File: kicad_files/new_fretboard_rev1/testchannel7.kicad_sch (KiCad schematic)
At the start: 22 parts, among them U2 LX3302AQPW-TR-EASY

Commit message: all circuit traces
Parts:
- removed C12, C13: 680pf, Capacitor_SMD:C_0603_1608Metric, symbol Device:C
- removed C14, C15: 10pf, Capacitor_SMD:C_0402_1005Metric, symbol Device:C
- removed C16: 1uf, Capacitor_SMD:C_0603_1608Metric, symbol Device:C
- removed C17, C20: 100nf, Capacitor_SMD:C_0402_1005Metric, symbol Device:C
- removed C18, C19: 6.8nf, Capacitor_SMD:C_0402_1005Metric, symbol Device:C
- removed C21: 1000pf, Capacitor_SMD:C_0402_1005Metric, symbol Device:C
- removed C22: 470nf, Capacitor_SMD:C_0402_1005Metric, symbol Device:C
- removed L5, L6, L7, L8: L, NetTie:NetTie-2_SMD_Pad0.5mm, symbol Device:L
- removed R10, R11, R8, R9: 10R, Resistor_SMD:R_0402_1005Metric, symbol Device:R
- removed R12: 221R, Resistor_SMD:R_0402_1005Metric, symbol Device:R
- removed R13: 4.7R, Resistor_SMD:R_0402_1005Metric, symbol Device:R
- removed U2: LX3302AQPW-TR-EASY, Snapeda:14-TSSOP_MCH-L, symbol Snapeda:LX3302AQPW-TR-EASY
- added C78, C84: 100nf, Capacitor_SMD:C_0402_1005Metric, symbol Device:C
- added C79: 1000pf, Capacitor_SMD:C_0402_1005Metric, symbol Device:C
- added C80: 470nf, Capacitor_SMD:C_0402_1005Metric, symbol Device:C
- added C81: 1uf, Capacitor_SMD:C_0603_1608Metric, symbol Device:C
- added C82, C83: 6.8nf, Capacitor_SMD:C_0402_1005Metric, symbol Device:C
- added C85, C86: 10pf, Capacitor_SMD:C_0402_1005Metric, symbol Device:C
- added C87, C88: 680pf, Capacitor_SMD:C_0603_1608Metric, symbol Device:C
- added L29, L30, L31, L32: L, NetTie:NetTie-2_SMD_Pad0.5mm, symbol Device:L
- added R43: 4.7R, Resistor_SMD:R_0402_1005Metric, symbol Device:R
- added R44: 221R, Resistor_SMD:R_0402_1005Metric, symbol Device:R
- added R45, R46, R47, R48: 10R, Resistor_SMD:R_0402_1005Metric, symbol Device:R
- added U8: LX3302AQPW-TR-EASY, Snapeda:14-TSSOP_MCH-L, symbol Snapeda:LX3302AQPW-TR-EASY
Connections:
- net CL1B_A: now also L32.1, R48.2
- net CL1_A: now also C85.1, R48.1, U8.8 (CL1)
- net CL2B_A: now also L31.1, R47.2
- net CL2_A: now also C86.1, R47.1, U8.10 (CL2)
- net GND: now also C78.1, C79.1, C80.1, C81.1, C82.1, C83.1, C85.2, C86.2, C87.2, C88.2, L31.2, L32.2, U8.2 (GND), U8.9 (GNDCL)
- net OSC11_A: now also C87.1, L29.2, U8.13 (OSC1)
- net OSC12_A: now also C88.1, L30.2, U8.12 (OSC2)
- net SUB_A: now also C84.1, U8.11 (SUB)
- net VIN_A: now also C79.2, C80.2, R43.1, R45.2, R46.1, U8.4 (VIN)
- new net: C81.2, C84.2, U8.5 (VDD)
- new net: C78.2, R43.2
- new net: C83.2, R44.1, R45.1, U8.6 (IO2)
- new net: C82.2, R44.2
- new net /OSC2B_A: L29.1, L30.1, R46.2
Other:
- removed sheet testchannel1
- removed sheet testchannel2
- removed sheet testchannel3
- removed sheet testchannel4
- removed sheet testchannel5
- removed sheet testchannel6
- removed sheet testchannel7

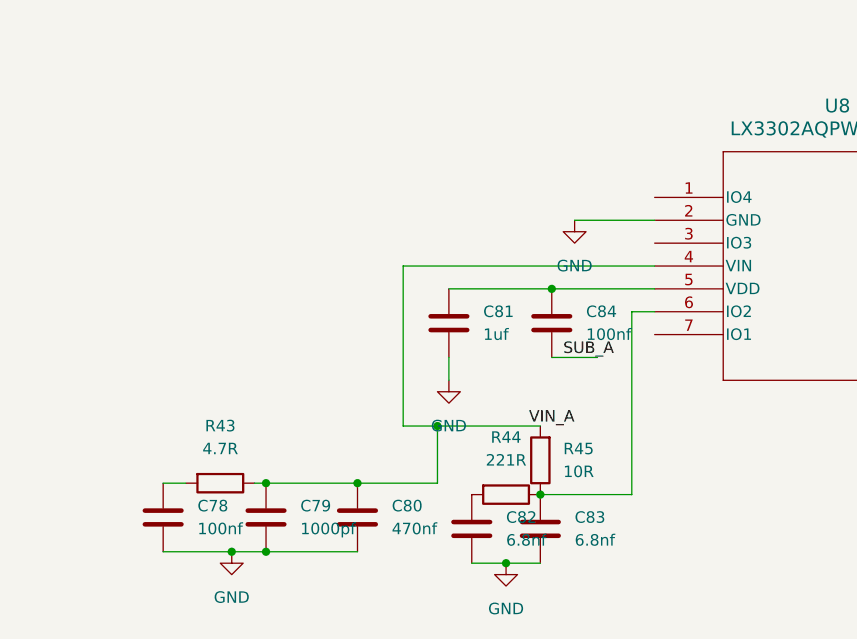
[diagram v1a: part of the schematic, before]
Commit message: stm32 micro added
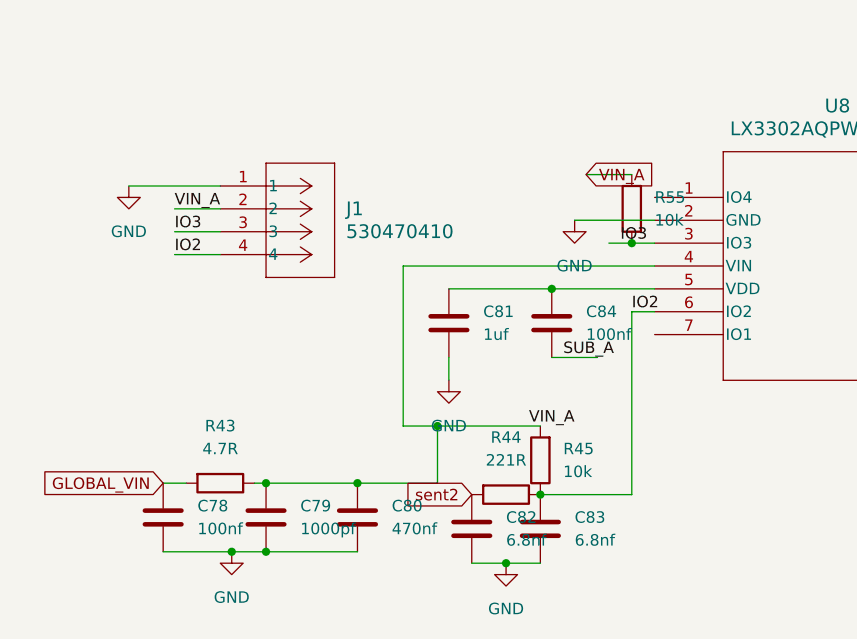
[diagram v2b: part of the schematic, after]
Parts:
- added J1: 530470410, Snapeda:CONN04_530470410_MOL, symbol Snapeda:530470410
- added R55: 10k, Resistor_SMD:R_0402_1005Metric, symbol Device:R
- R45: value 10R -> 10k
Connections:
- net GND: now also J1.1
- net VIN_A: now also J1.2, R55.2
- net GLOBAL_VIN: now reaches C78.2, R43.2
- net IO3: now reaches U8.3 (IO3)
- net IO3: now also J1.3, R55.1
- net IO2: now reaches C83.2, R44.1, R45.1, U8.6 (IO2)
- net IO2: now also J1.4
- net sent2: now reaches C82.2, R44.2

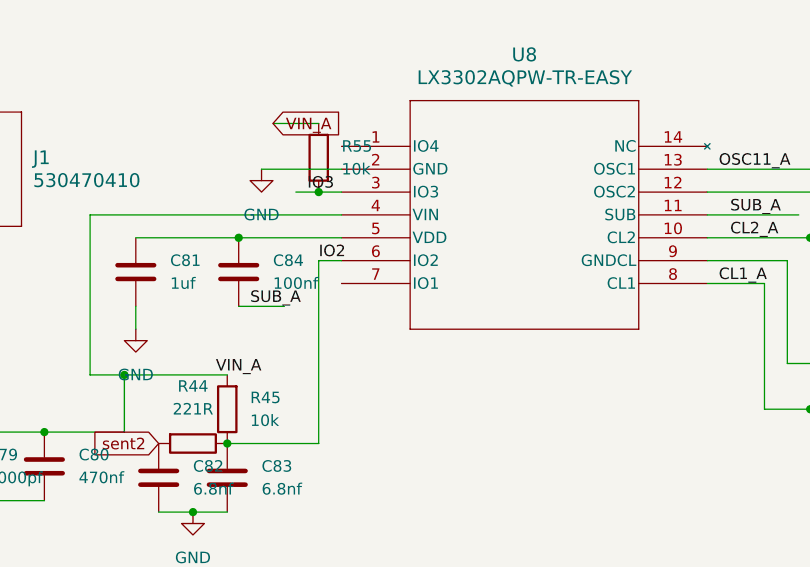
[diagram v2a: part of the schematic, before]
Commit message: mcu configured, still needs power connections and spi i2c connections
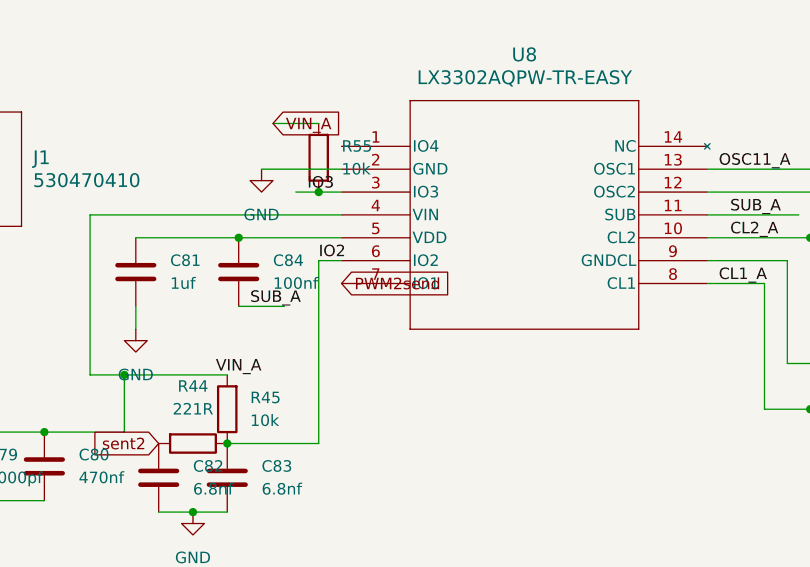
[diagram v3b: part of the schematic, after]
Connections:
- net PWM2send: now reaches U8.7 (IO1)
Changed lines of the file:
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@@
+		)
+	)
+	(global_label "PWM2send"
+		(shape input)
+		(at 104.14 106.68 0)
+		(fields_autoplaced yes)
+		(effects
+			(font
+				(size 1.27 1.27)
+			)
+			(justify left)
+		)
+		(property "Intersheetrefs" "${INTERSHEET_REFS}"
+			(at 116.9222 106.68 0)
+			(effects
+				(font
+					(size 1.27 1.27)
+				)
+				(justify left)
+				(hide yes)
+			)
 		)
 	)

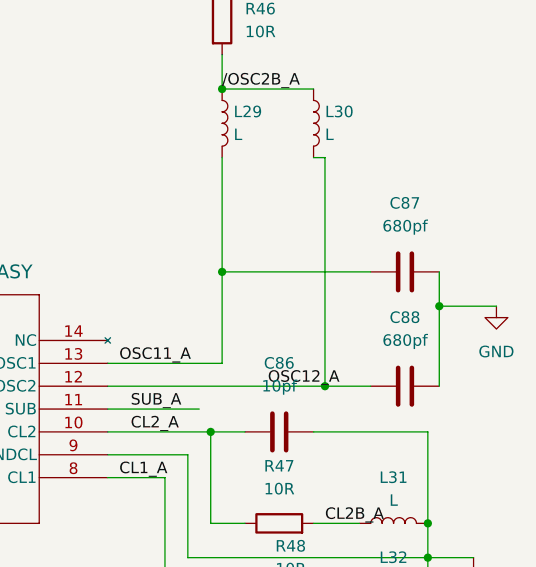
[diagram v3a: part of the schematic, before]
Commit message: finished routing - adding silkscreen
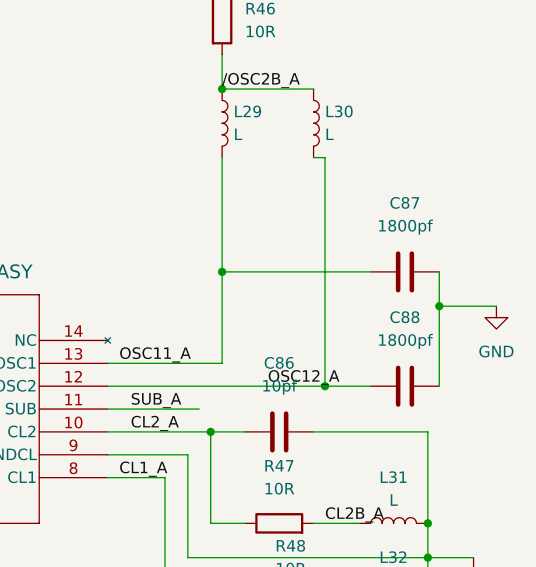
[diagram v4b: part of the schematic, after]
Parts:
- C87, C88: value 680pf -> 1800pf
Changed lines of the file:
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@@
 			)
 		)
-		(property "Value" "680pf"
+		(property "Value" "1800pf"
 			(at 177.8 78.74 90)
 			(effects
@@
 			)
 		)
-		(property "Value" "680pf"
+		(property "Value" "1800pf"
 			(at 177.8 91.44 90)
 			(effects

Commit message: exported gerbers of lefthand
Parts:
- L29, L30, L31, L32: now left out of the parts list
